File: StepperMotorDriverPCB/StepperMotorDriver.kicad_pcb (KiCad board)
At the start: 4 copper layers, 44 x 38.5 mm, 63 parts, among them IC2 TMC2209-LA, J1 Conn_01x02_Pin, J10 USB_C_Receptacle_USB2.0_16P, J2 Conn_01x01_Pin, J3 Conn_01x01_Pin, J4 Conn_01x04_Socket, J7 Conn_01x02_Pin, J8 Conn_01x01_Pin, J9 Conn_01x01_Pin, SW2 SW_SPST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

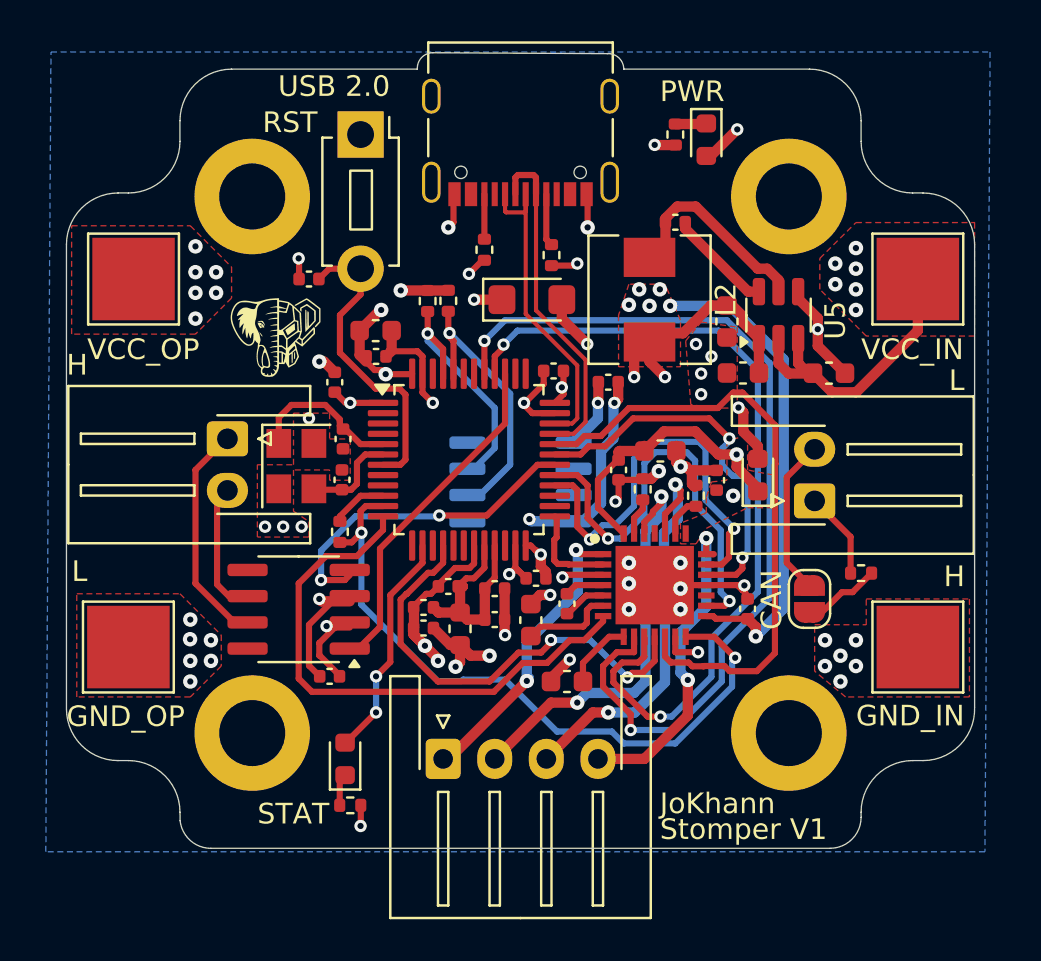
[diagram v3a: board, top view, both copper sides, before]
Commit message: Major Structural Updates.
Updated mounting hardware and PD
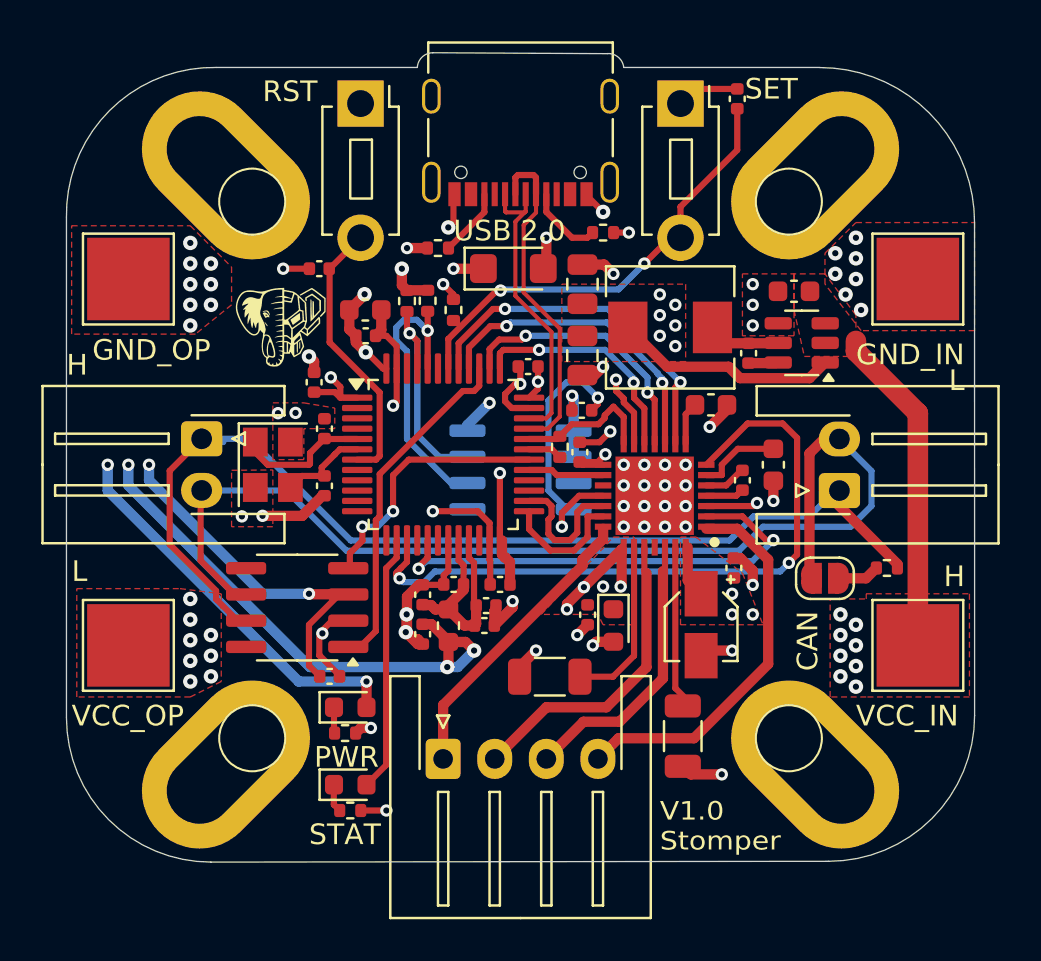
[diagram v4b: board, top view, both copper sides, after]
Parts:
- added C23: 0.1u, Capacitor_SMD:C_0402_1005Metric, F.Cu at (83.8, 44.8)
- added R1: 1k5, Resistor_SMD:R_0402_1005Metric, F.Cu at (70.0, 55.0)
- added SW1: SW_SPST, Button_Switch_THT:SW_PUSH_1P1T_6x3.5mm_H5.0_APEM_MJTP1250, F.Cu at (81.0, 45.0)
- C27, C28: footprint Capacitor_SMD:C_0603_1608Metric -> Capacitor_SMD:C_0805_2012Metric
- C8: footprint Capacitor_SMD:C_0603_1608Metric -> Capacitor_SMD:CP_Elec_3x5.3
- R5, R6: footprint Resistor_SMD:R_0402_1005Metric -> Resistor_SMD:R_1206_3216Metric
- moved R9 33.1 mm to (64.8, 75.5), turned to 0 degrees
- moved D3 32.5 mm to (65.0, 74.2), turned to 0 degrees
- moved J2 17.8 mm to (54.2, 53.5)
- moved J9 17.8 mm to (92.5, 53.5)
- moved J8 17.8 mm to (54.2, 71.2)
- moved J3 17.8 mm to (92.5, 71.2)
- moved C11 15.1 mm to (82.5, 59.6), turned to 180 degrees
- moved C10 14.0 mm to (85.5, 62.5), turned to 90 degrees
- moved R5 12.1 mm to (81.1, 75.6), turned to 90 degrees
- moved R4 11.4 mm to (75.2, 61.6), turned to -90 degrees
- moved R6 11.3 mm to (74.7, 72.8), turned to 0 degrees
- moved C5 11.1 mm to (76.1, 61.9)
- moved C6 10.4 mm to (84.0, 63.2), turned to 90 degrees
- moved D2 10.1 mm to (77.8, 70.3), turned to -90 degrees
- moved C9 9.03 mm to (76.5, 69.8), turned to -90 degrees
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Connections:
- C20 pad 1: Net-(SW2-B) -> GND
- C20 pad 2: GND -> Net-(SW2-B)
- J4 pad 1: /OB2 -> /OA2
- J4 pad 2: /OB1 -> /OA1
- J4 pad 3: /OA1 -> /OB1
- J4 pad 4: /OA2 -> /OB2
- U3 pad 10: /MOT_UART_TX -> unconnected-(U3-PA2-Pad10)
- U3 pad 11: /MOT_UART_RX -> unconnected-(U3-PA3-Pad11)
- U3 pad 12: /MOT_SPREAD -> unconnected-(U3-PA4-Pad12)
- U3 pad 15: unconnected-(U3-PA7-Pad15) -> /MOT_SPREAD
- U3 pad 16: /MOT_DIAG -> unconnected-(U3-PB0-Pad16)
- U3 pad 17: unconnected-(U3-PB1-Pad17) -> /MOT_ENABLE
- U3 pad 25: /MOT_ENABLE -> /MOT_STBY
- U3 pad 26: unconnected-(U3-PB12-Pad26) -> /MOT_DIR
- U3 pad 28: /MOT_STBY -> unconnected-(U3-PB14-Pad28)
- U3 pad 31: /MOT_DIR -> /MOT_UART_TX
- U3 pad 32: /MOT_INDEX -> /MOT_UART_RX
- U3 pad 37: unconnected-(U3-PA13-Pad37) -> /MOT_INDEX
- U3 pad 38: unconnected-(U3-PA14-Pad38) -> /MOT_DIAG
- U3 pad 42: unconnected-(U3-PB5-Pad42) -> Net-(SW1-B)
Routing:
- net +3V3: track 68.3 -> 102.1 mm, vias 20 -> 24
- net /MOT_MS1: track 44.9 -> 17.3 mm
- net /MOT_UART_RX: track 33.2 -> 6.84 mm, vias 2 -> 0
- net /MOT_MS2: track 40.6 -> 15.3 mm
- net Net-(SW1-B): track 0.00 -> 22.1 mm, vias 0 -> 2
- net /MOT_INDEX: track 30.4 -> 11.3 mm, vias 0 -> 2
- net /MOT_ENABLE: track 4.67 -> 23.1 mm, vias 0 -> 2
- net /MOT_STEP: track 21.1 -> 3.69 mm, vias 2 -> 0
- net /MOT_STBY: track 20.1 -> 6.15 mm, vias 2 -> 0
- net /MOT_DIR: track 18.8 -> 6.65 mm, vias 2 -> 0
- net /MOT_DIAG: track 22.0 -> 13.1 mm
- net Net-(U5-SW): track 9.96 -> 2.36 mm
- net /OB1: track 20.5 -> 13.7 mm, vias 2 -> 0
- net Net-(IC2-BRA): track 1.98 -> 8.29 mm
- net /MOT_SPREAD: track 27.1 -> 33.2 mm, vias 0 -> 2
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- added copper zone on In2.Cu, net +3V3
- removed copper zone on B.Cu, net +3V3
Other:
- board size 44 x 38.5 mm -> 44 x 39.2 mm
- board text added: "JoKhann 08/29/24"
- board text added: "SET"
- board text added: "V1.0 Stomper"
- board text removed: "JoKhann"
- board text removed: "Stomper V1"

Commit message: Updates to circuitry
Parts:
- added J5: Conn_01x02_Pin, Connector_PinHeader_2.00mm:PinHeader_1x02_P2.00mm_Vertical, F.Cu at (73.1, 73.8)
- added JP2: Jumper_2_Bridged, Jumper:SolderJumper-2_P1.3mm_Open_RoundedPad1.0x1.5mm, F.Cu at (64.2, 56.0)
- added R12: 10k, Resistor_SMD:R_0402_1005Metric, F.Cu at (62.5, 56.8)
- C8: footprint Capacitor_SMD:CP_Elec_3x5.3 -> Capacitor_THT:CP_Radial_D5.0mm_P2.50mm
- J2, J3, J8, J9: footprint TestPoint:TestPoint_Pad_4.0x4.0mm -> TestPoint:TestPoint_Plated_Hole_D2.0mm
- R1: value 1k5 -> 10k
- moved R1 8.93 mm to (78.5, 52.2), turned to 0 degrees
- moved R2 5.75 mm to (73.2, 56.2)
- moved C25 4.04 mm to (89.8, 56.5), turned to -90 degrees
- moved J3 2.36 mm to (90.5, 72.5)
- moved J8 2.15 mm to (56.0, 72.5)
- moved J9 2.06 mm to (90.5, 53.0)
- moved J2 1.82 mm to (56.0, 53.0)
- moved R6 1.67 mm to (75.8, 71.5), turned to -90 degrees
- moved G*** 1.27 mm to (60.5, 55.5)
- moved C15 1.27 mm to (67.0, 55.0)
- moved C9 1.13 mm to (76.0, 68.8), turned to 180 degrees
- moved C16 0.99 mm to (66.7, 56.3)
- moved R11 0.79 mm to (90.2, 67.8), turned to 90 degrees
- moved D2 0.79 mm to (77.8, 69.5)
- moved R9 0.75 mm to (65.5, 75.5)
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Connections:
- U3 pad 2: unconnected-(U3-PC13-Pad2) -> Net-(SW1-B)
- U3 pad 37: /MOT_INDEX -> /SWDIO
- U3 pad 38: /MOT_DIAG -> /SWCLK
- U3 pad 39: /CAN_TX -> /ESCL
- U3 pad 40: /MOT_MS2 -> /MOT_INDEX
- U3 pad 41: /MOT_MS1 -> /CAN_TX
- U3 pad 42: Net-(SW1-B) -> /MOT_DIAG
- U3 pad 43: unconnected-(U3-PB6-Pad43) -> /MOT_MS2
- U3 pad 45: /ESCL -> Net-(JP2-B)
- U3 pad 46: unconnected-(U3-PB9-Pad46) -> /MOT_MS1
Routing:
- net /SWCLK: track 0.00 -> 52.1 mm, vias 0 -> 1
- net /SWDIO: track 0.00 -> 50.4 mm, vias 0 -> 1
- net +3V3: track 102.1 -> 78.2 mm, vias 24 -> 23
- net Net-(JP2-B): track 0.00 -> 7.88 mm
- net Net-(SW1-B): track 22.1 -> 29.4 mm
- net GND: track 82.5 -> 89.7 mm, vias 68 -> 46
- net VCC: track 25.3 -> 21.8 mm, vias 24 -> 7
- net /MOT_DIR: track 6.65 -> 3.69 mm
- net /MOT_SPREAD: track 33.2 -> 30.4 mm
- net /MOT_STBY: track 6.15 -> 3.69 mm
- net /MOT_MS1: track 17.3 -> 19.6 mm
- net Net-(SW2-B): track 13.9 -> 15.7 mm, vias 0 -> 2
- net /ESDA: track 14.1 -> 12.4 mm
- net /MOT_DIAG: track 13.1 -> 14.7 mm
- net /MOT_MS2: track 15.3 -> 16.7 mm
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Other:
- board size 44 x 39.2 mm -> 40.3 x 39.2 mm
- board text added: "B0"
- board text added: "CLK IO"
- board text added: "GND_I"
- board text added: "GND_O"
- board text added: "JoKhann 09/15/24"
- board text added: "SWD"
- board text added: "V1.1 Stomper"
- board text added: "VCC_I"
- board text added: "VCC_O"
- board text removed: "GND_IN"
- board text removed: "GND_OP"
- board text removed: "JoKhann 08/29/24"
- board text removed: "V1.0 Stomper"
- board text removed: "VCC_IN"
- board text removed: "VCC_OP"
